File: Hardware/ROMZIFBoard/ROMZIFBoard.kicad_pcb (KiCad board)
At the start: 4 copper layers, 62 x 32.3 mm, 4 parts, among them J1 LowerHeader, J2 UpperHeader, U1 M29F400FB55N3F2

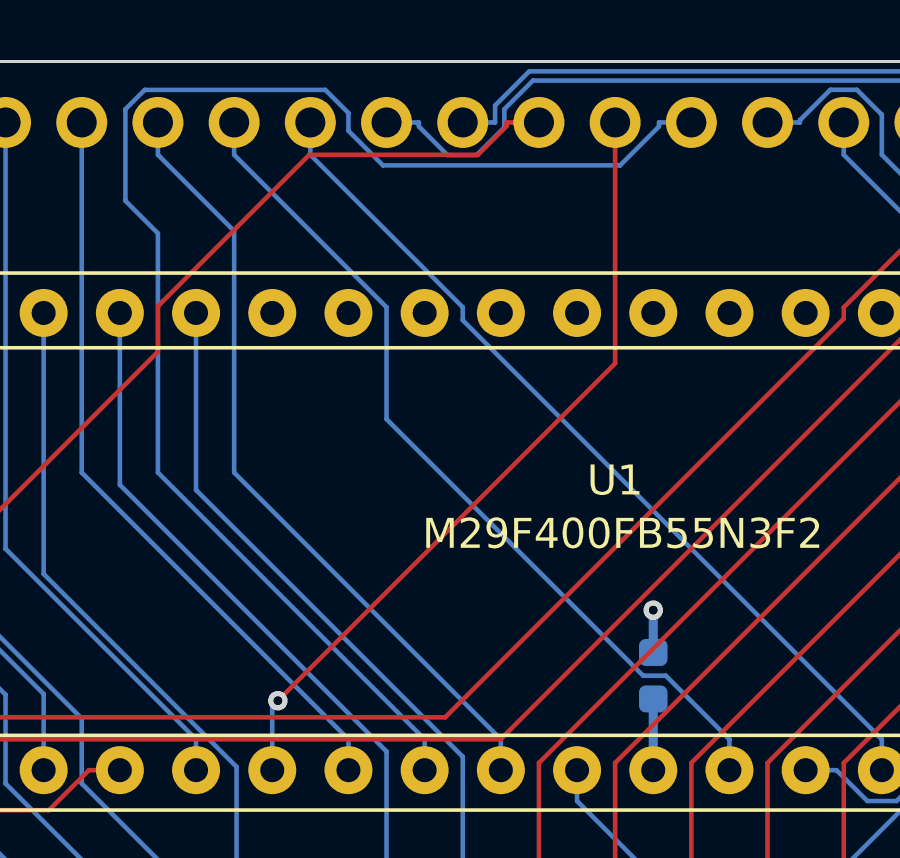
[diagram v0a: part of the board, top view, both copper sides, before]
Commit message: Update all KiCAD projects to KiCAD 9
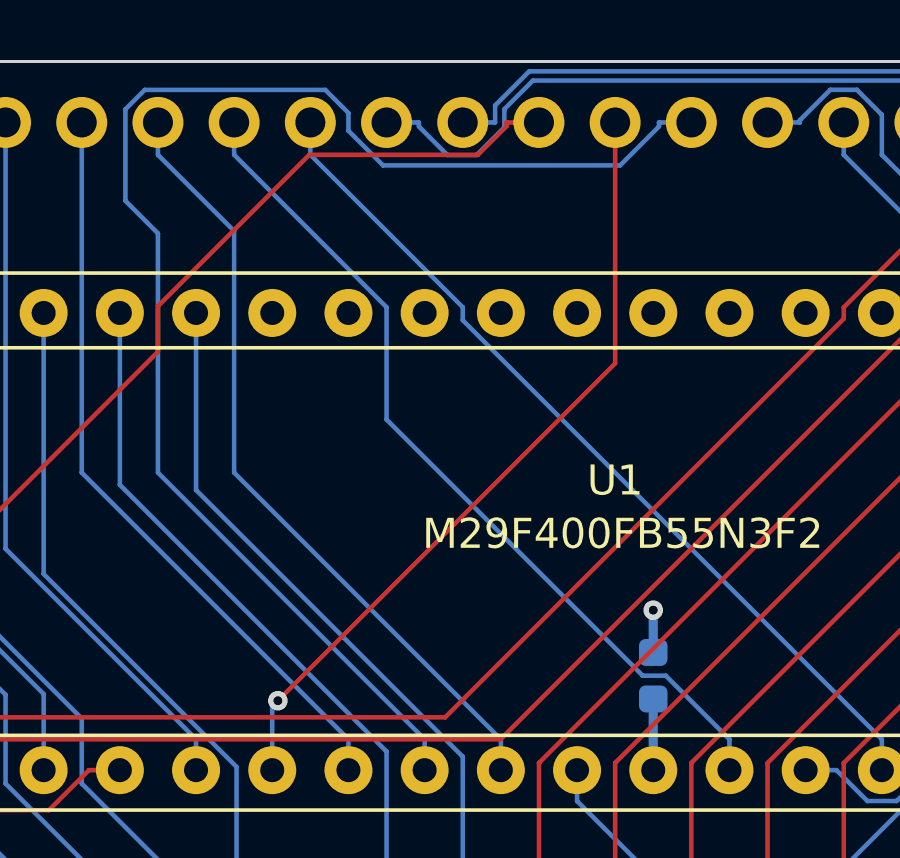
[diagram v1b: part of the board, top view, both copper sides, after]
